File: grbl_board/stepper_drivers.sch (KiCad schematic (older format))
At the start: 46 parts, among them J6 X_STEPPER, J7 Y_STEPPER, J8 Z_STEPPER, J9 E_STEPPER, U5 TMC5160_SILENTSTEPSTICK, U6 TMC5160_SILENTSTEPSTICK, U7 TMC5160_SILENTSTEPSTICK, U8 TMC5160_SILENTSTEPSTICK

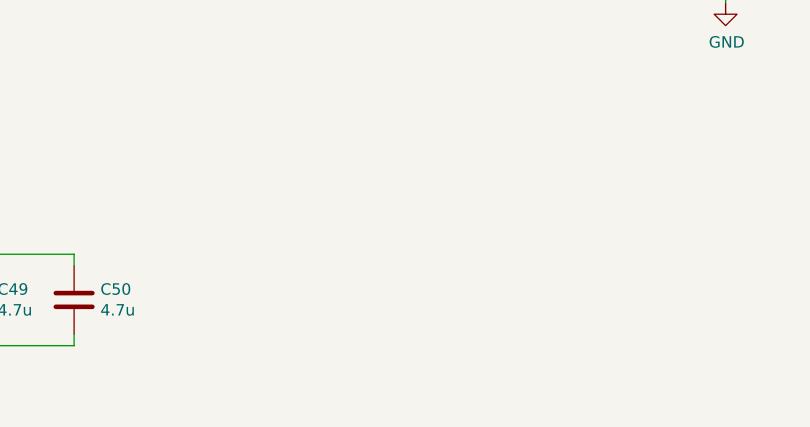
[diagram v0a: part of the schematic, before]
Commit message: fixed pullup resistors on board, and 5v regulator overheating, and stepper driver flipped
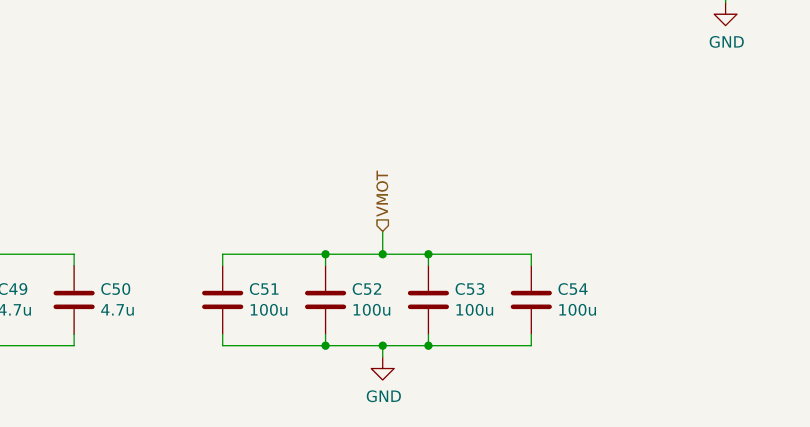
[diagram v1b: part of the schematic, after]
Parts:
- added C51, C52, C53, C54: 100u, Capacitor_SMD:CP_Elec_8x10, symbol Device:C
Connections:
- net GND: now also C51.2, C52.2, C53.2, C54.2
- net VMOT: now also C51.1, C52.1, C53.1, C54.1

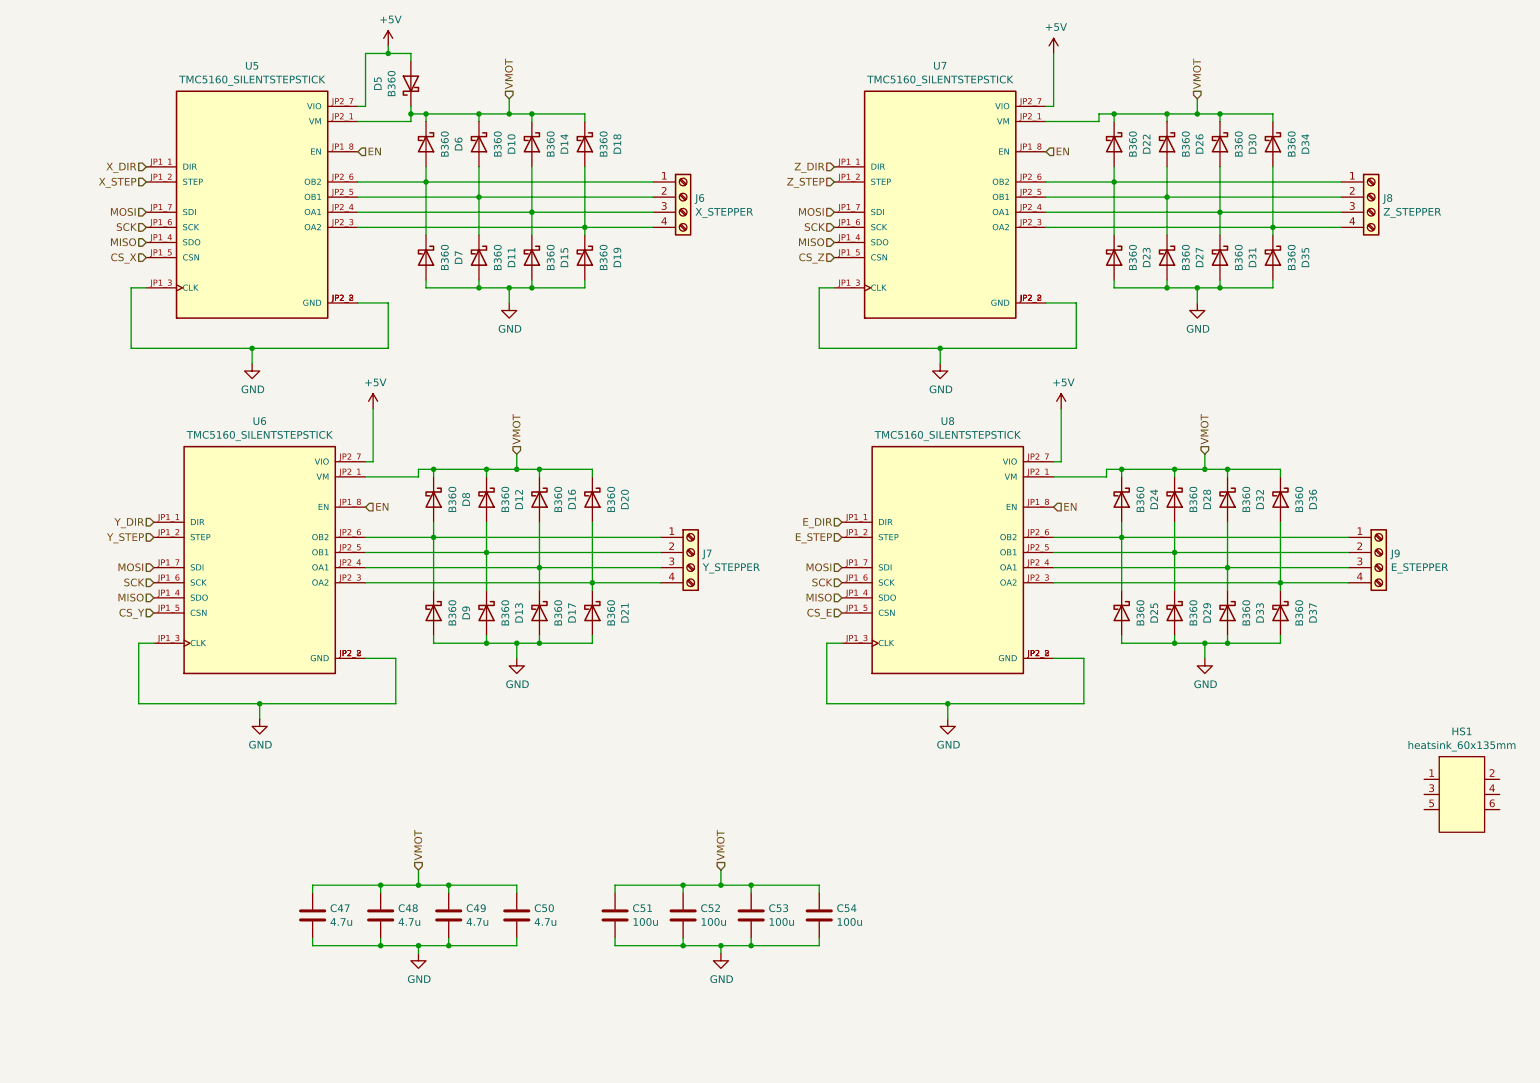
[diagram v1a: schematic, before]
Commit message: updated board with 24V reg
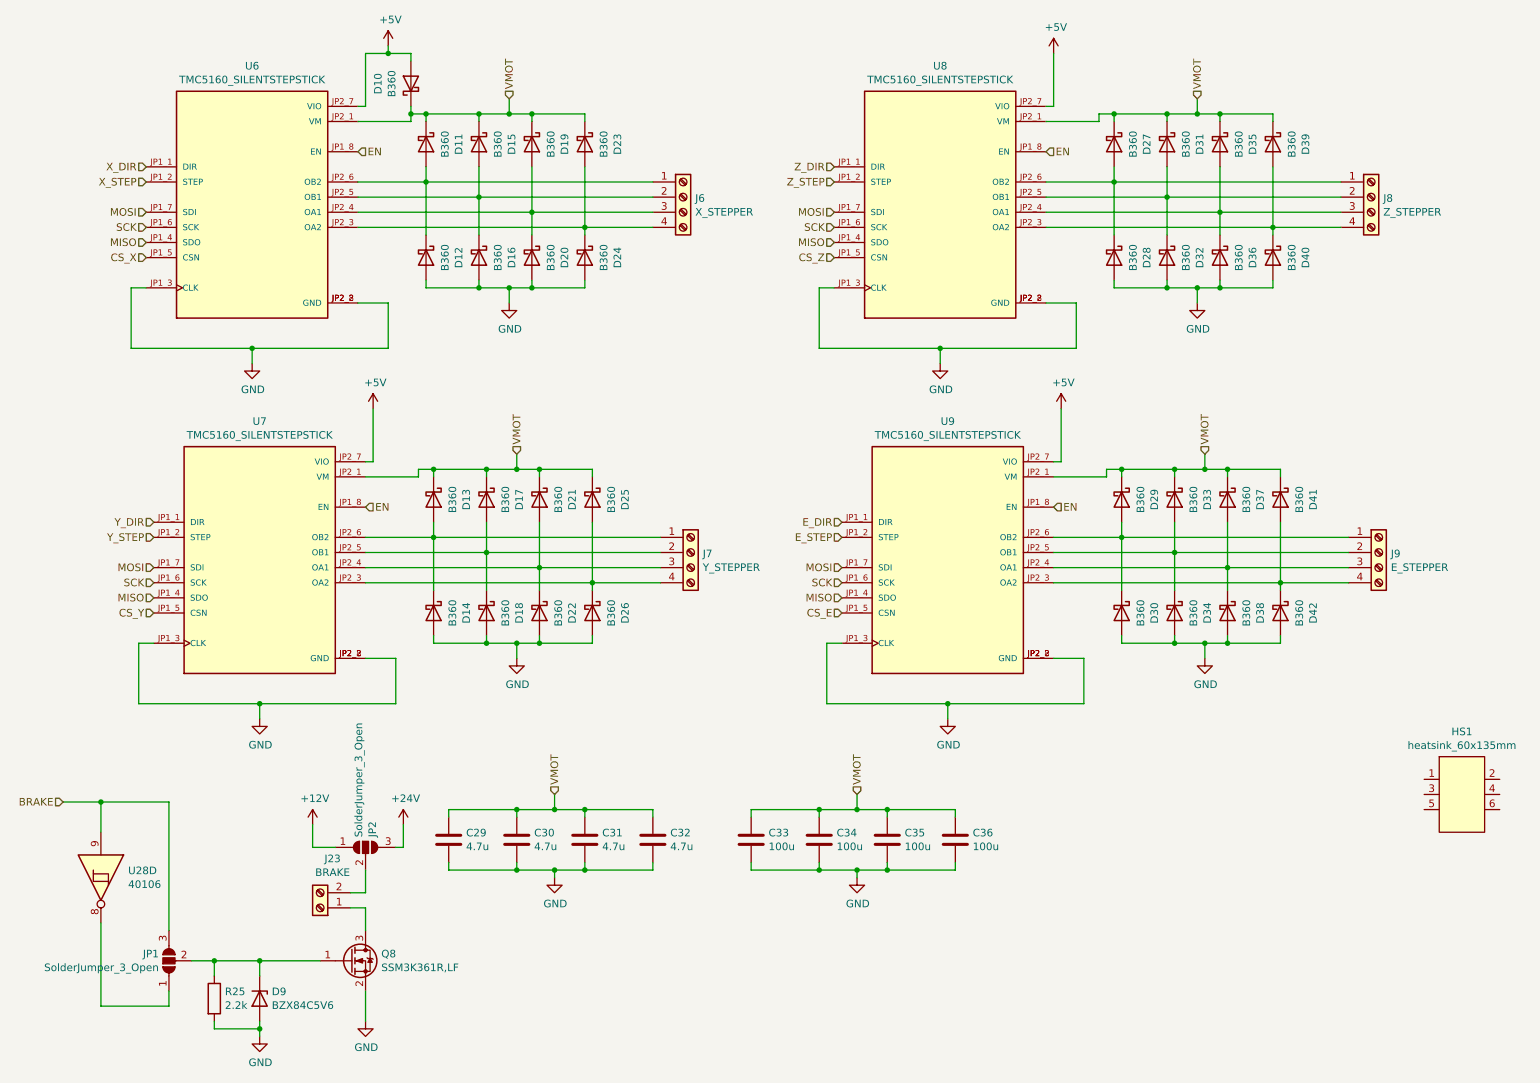
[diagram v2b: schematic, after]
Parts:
- added D9: BZX84C5V6, Diode_SMD:D_SOT-23_ANK, symbol Diode:BZX84Cxx
- added J23: BRAKE, Connector_Phoenix_MC:PhoenixContact_MC_1,5_2-G-3.81_1x02_P3.81mm_Horizontal, symbol Connector:Screw_Terminal_01x02
- added JP1, JP2: SolderJumper_3_Open, Jumper:SolderJumper-3_P1.3mm_Open_RoundedPad1.0x1.5mm, symbol Jumper:SolderJumper_3_Open
- added Q8: SSM3K361R,LF, Package_TO_SOT_SMD:SOT-23, symbol Device:Q_NMOS_GSD
- added R25: 2.2k, Resistor_SMD:R_0603_1608Metric_Pad0.98x0.95mm_HandSolder, symbol Device:R
- added U28: 40106, symbol 4xxx:40106
- renumbered C47 to C29, C48 to C30, C49 to C31, C50 to C32, C51 to C33, C52 to C34, C53 to C35, C54 to C36, D5 to D10, D6 to D11, D7 to D12, D8 to D13, D9 to D14, D10 to D15, D11 to D16, D12 to D17, D13 to D18, D14 to D19, D15 to D20, D16 to D21, D17 to D22, D18 to D23, D19 to D24, D20 to D25, D21 to D26, D22 to D27, D23 to D28, D24 to D29, D25 to D30, D26 to D31, D27 to D32, D28 to D33, D29 to D34, D30 to D35, D31 to D36, D32 to D37, D33 to D38, D34 to D39, D35 to D40, D36 to D41, D37 to D42, U5 to U6, U6 to U7, U7 to U8, U8 to U9
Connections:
- net GND: now also D9.2 (A), Q8.2 (S), R25.2
- new net: JP1.1 (A), U28.8
- new net: D9.1 (K), JP1.2 (C), Q8.1 (G), R25.1
- new net: J23.1 (Pin_1), Q8.3 (D)
- new net: J23.2 (Pin_2), JP2.2 (C)
- new net +12V: JP2.1 (A)
- new net +24V: JP2.3 (B)
- new net BRAKE: JP1.3 (B), U28.9
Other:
- moved on the sheet: C29, C30, C31, C32, C33, C34, C35, C36
